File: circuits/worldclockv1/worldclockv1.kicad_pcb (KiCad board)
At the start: 2 copper layers, 152.4 x 76.2 mm, 98 parts, among them J1 Rotary Encoder Module, J2 UART, J3 Power, J4 Display 1 A, J5 Display 2 A, J6 Display 3 A, J7 Display 1 B, J8 Display 2 B, J9 Display 3 B, Q1 BSS138, Q2 BSS138, Q3 BSS138, Q4 BSS138, Q5 BSS138, Q6 BSS138, SW1 EN, SW2 BOOT, U1 ESP32-WROOM-32UE, U2 DS3232M, U3 LD1117S33TR_SOT223, U4 L7805, U5 L7805, U6 L7805, U7 LM386

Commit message: World Clock PCB completed
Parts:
- added C18: 100 nF, Capacitor_SMD:C_1206_3216Metric_Pad1.33x1.80mm_HandSolder, F.Cu at (201.7, 119.4)
- added F1: Polyfuse, Fuse:Fuseholder_Littelfuse_Nano2_157x, F.Cu at (195.6, 138.9)
- added Hole1: MountingHole_3.2mm_M3, MountingHole:MountingHole_3.2mm_M3, F.Cu at (46.2, 43.7)
- added Hole2: MountingHole_3.2mm_M3, MountingHole:MountingHole_3.2mm_M3, F.Cu at (229.9, 43.7)
- added Hole3: MountingHole_3.2mm_M3, MountingHole:MountingHole_3.2mm_M3, F.Cu at (46.2, 153.4)
- added Hole4: MountingHole_3.2mm_M3, MountingHole:MountingHole_3.2mm_M3, F.Cu at (229.9, 153.5)
- added J10: BOOT, Connector_PinHeader_2.54mm:PinHeader_1x02_P2.54mm_Vertical, F.Cu at (228.3, 95.8)
- added JP10: ID_WP, Jumper:SolderJumper-2_P1.3mm_Open_RoundedPad1.0x1.5mm, F.Cu at (189.1, 135.6)
- added JP7: ID_WP, Jumper:SolderJumper-2_P1.3mm_Open_RoundedPad1.0x1.5mm, F.Cu at (63.5, 73.2)
- added JP8: ID_WP, Jumper:SolderJumper-2_P1.3mm_Open_RoundedPad1.0x1.5mm, F.Cu at (63.5, 107.0)
- added JP9: ID_WP, Jumper:SolderJumper-2_P1.3mm_Open_RoundedPad1.0x1.5mm, F.Cu at (63.5, 141.2)
- added Q7: IRLML6402, Package_TO_SOT_SMD:SOT-23, F.Cu at (189.0, 141.8)
- added R23: 100k, Resistor_SMD:R_1206_3216Metric_Pad1.30x1.75mm_HandSolder, F.Cu at (189.0, 147.6)
- added R24: 10k, Resistor_SMD:R_1206_3216Metric_Pad1.30x1.75mm_HandSolder, F.Cu at (191.0, 112.8)
- added R25: 10k, Resistor_SMD:R_1206_3216Metric_Pad1.30x1.75mm_HandSolder, F.Cu at (191.0, 103.4)
- added R26: 10k, Resistor_SMD:R_1206_3216Metric_Pad1.30x1.75mm_HandSolder, F.Cu at (221.0, 116.1)
- added SW3: RotaryEncoder_Switch, Rotary_Encoder:RotaryEncoder_Alps_EC11E-Switch_Vertical_H20mm, F.Cu at (195.1, 105.7)
- added SW4: Alt, Button_Switch_THT:SW_PUSH_6mm, F.Cu at (214.5, 106.0)
- added TP25: GND, TestPoint:TestPoint_Loop_D2.50mm_Drill1.0mm, F.Cu at (87.4, 152.1)
- added TP26: GND, TestPoint:TestPoint_Loop_D2.50mm_Drill1.0mm, F.Cu at (95.8, 152.1)
- added TP27: GND, TestPoint:TestPoint_Loop_D2.50mm_Drill1.0mm, F.Cu at (104.3, 152.1)
- added TP28: GND, TestPoint:TestPoint_Loop_D2.50mm_Drill1.0mm, F.Cu at (112.8, 152.1)
- J3: footprint Connector_PinSocket_2.54mm:PinSocket_1x02_P2.54mm_Vertical -> Connector_BarrelJack:BarrelJack_Horizontal
- SW1, SW2: footprint Connector_PinSocket_2.54mm:PinSocket_1x02_P2.54mm_Vertical -> Button_Switch_THT:SW_PUSH_6mm
- moved TP15 524.4 mm to (185.2, 151.9)
- moved TP16 514.9 mm to (176.8, 151.9)
- moved TP17 508.1 mm to (171.8, 151.9)
- moved JP2 501.3 mm to (167.9, 151.9), turned to 180 degrees
- moved TP21 500.8 mm to (163.9, 151.9)
- moved J3 500.0 mm to (203.8, 144.1), turned to 90 degrees
- moved U3 498.1 mm to (149.4, 151.9), turned to 180 degrees
- moved JP1 497.5 mm to (181.0, 151.9), turned to 180 degrees
- moved C4 468.1 mm to (157.8, 151.8), turned to -90 degrees
- moved RV1 443.1 mm to (230.4, 85.8), turned to 180 degrees
- moved C8 441.9 mm to (140.2, 152.7), turned to -90 degrees
- moved RV2 437.4 mm to (217.2, 83.3), turned to 90 degrees
- moved TP20 429.6 mm to (66.0, 151.4)
- moved JP5 414.0 mm to (62.1, 151.4), turned to 180 degrees
- moved TP24 410.8 mm to (57.9, 151.4)
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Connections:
- net Net-(J1-Pin_1) renamed /Rotary Encoder Module/CLK
- net Net-(J1-Pin_2) renamed /Rotary Encoder Module/DT
- net Net-(J1-Pin_3) renamed /Rotary Encoder Module/SW
- JP1 pad 1: Net-(J3-Pin_1) -> Net-(JP1-A)
- R12 pad 1: +5V -> +5V #1
- R13 pad 1: +5V -> +5V #1
- R14 pad 1: +5V -> +5V #2
- R15 pad 1: +5V -> +5V #2
- R18 pad 1: +5V -> +5V #3
- R19 pad 1: +5V -> +5V #3
- TP15 pad 1: Net-(J3-Pin_1) -> Net-(JP1-A)
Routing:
- net +VDC: track 0.00 -> 452.5 mm
- net +3V3: track 0.00 -> 329.2 mm, vias 0 -> 10
- net +5V #1: track 0.00 -> 97.8 mm, vias 0 -> 3
- net +5V #2: track 0.00 -> 96.4 mm, vias 0 -> 3
- net +5V #3: track 0.00 -> 96.0 mm, vias 0 -> 3
- net /Rotary Encoder Module/DT: track 0.00 -> 86.9 mm, vias 0 -> 5
- net Net-(U1-IO26): track 0.00 -> 84.8 mm, vias 0 -> 4
- net /Rotary Encoder Module/SW: track 0.00 -> 84.2 mm, vias 0 -> 1
- net /Level Shifter/LV5: track 0.00 -> 78.8 mm
- net /Level Shifter/LV6: track 0.00 -> 78.6 mm
- net Net-(J10-Pin_1): track 0.00 -> 74.0 mm, vias 0 -> 3
- net Net-(U1-IO4): track 0.00 -> 73.0 mm, vias 0 -> 2
- net /Level Shifter/LV3: track 0.00 -> 72.9 mm, vias 0 -> 2
- net /Level Shifter/LV1: track 0.00 -> 72.9 mm
- net /Level Shifter/LV4: track 0.00 -> 70.7 mm, vias 0 -> 2
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- added copper zone on B.Cu, net GND
- added copper zone on F.Cu, net GND
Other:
- board size 152.4 x 76.2 mm -> 193.8 x 120 mm
- board text added: "3V3"
- board text added: "3V3 Current"
- board text added: "5V Current"
- board text added: "Audio"
- board text added: "Boot"
- board text added: "CLK"
- board text added: "DAC1"
- board text added: "DIO"
- board text added: "DT"
- board text added: "EN"
- board text added: "ESP32 World Clock v1.0"
- board text added: "GND"
- board text added: "GOS-WC-01 2026-04"
- board text added: "INT"
- board text added: "Mode"
- board text added: "Prog"
- board text added: "RST"
- board text added: "RX"
- board text added: "Reset"
- board text added: "Rot Enc"
- board text added: "SCL"
- board text added: "SDA"
- board text added: "SW"
- board text added: "TX"
- board text added: "Total Current"
- board text added: "© 2026 Geirmundur Orri Sigurdsson"

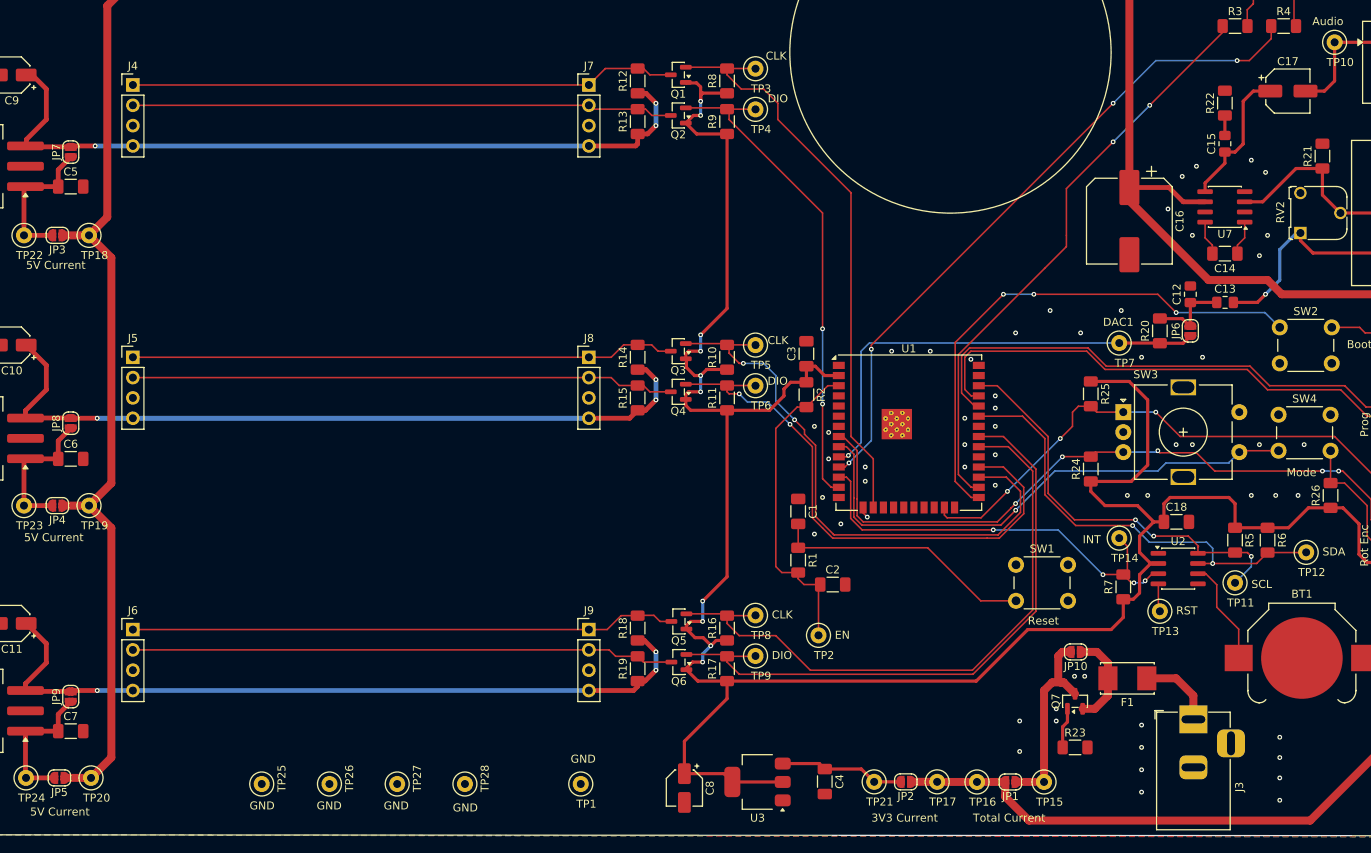
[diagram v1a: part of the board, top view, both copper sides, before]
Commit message: Update some caps footprint sizes for the World Clock
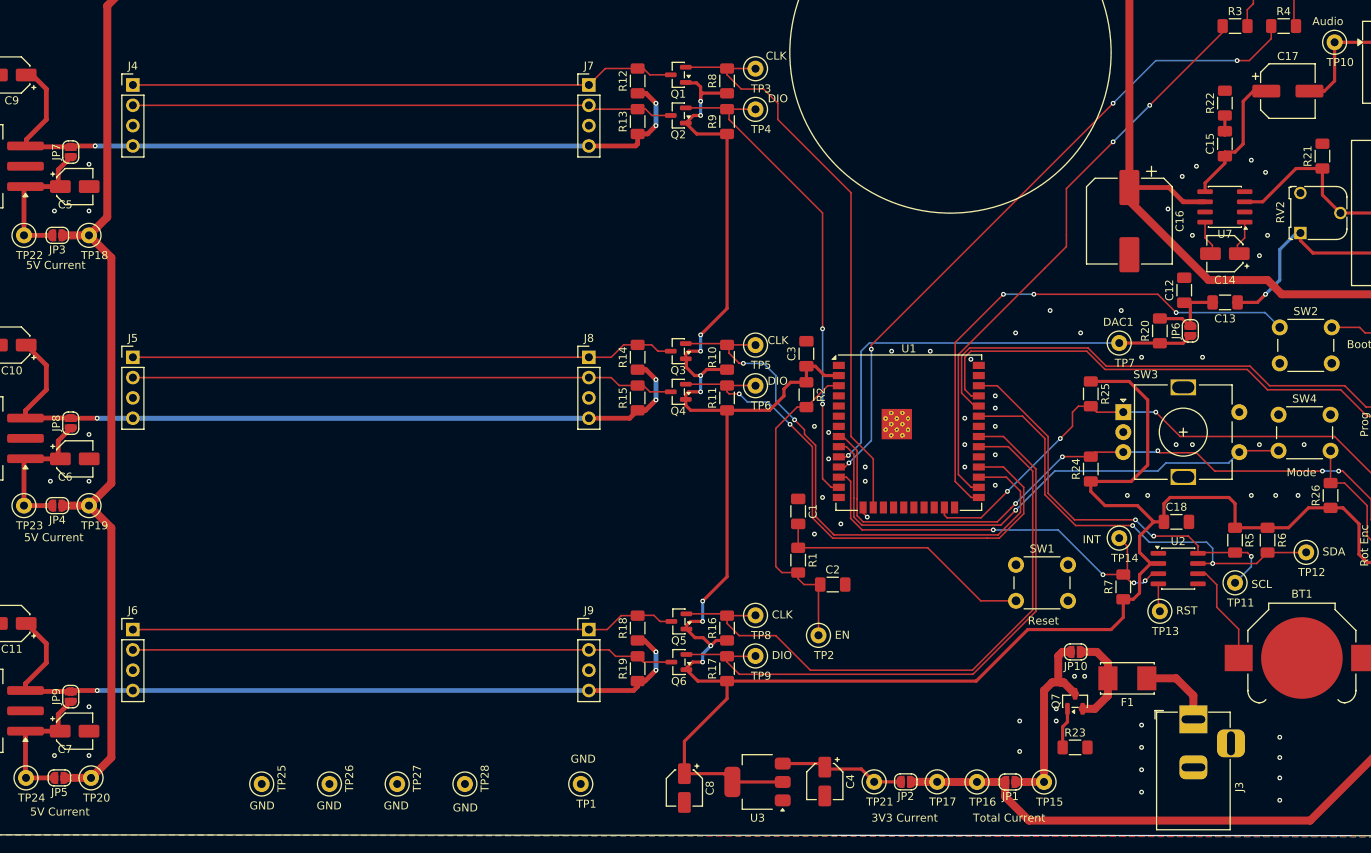
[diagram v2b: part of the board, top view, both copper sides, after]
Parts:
- C12, C13, C15: footprint Capacitor_SMD:C_0805_2012Metric_Pad1.18x1.45mm_HandSolder -> Capacitor_SMD:C_1206_3216Metric_Pad1.33x1.80mm_HandSolder
- C14, C4, C5, C6, C7: footprint Capacitor_SMD:C_1206_3216Metric_Pad1.33x1.80mm_HandSolder -> Capacitor_SMD:CP_Elec_4x5.4
- C17: footprint Capacitor_SMD:CP_Elec_5x5.4 -> Capacitor_SMD:CP_Elec_6.3x7.7
- moved C12 0.92 mm to (202.7, 90.4)
- moved C5 0.51 mm to (64.0, 77.5)
- moved C6 0.51 mm to (64.0, 111.5)
- moved C7 0.49 mm to (64.0, 145.5)
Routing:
- net GND: vias 63 -> 72

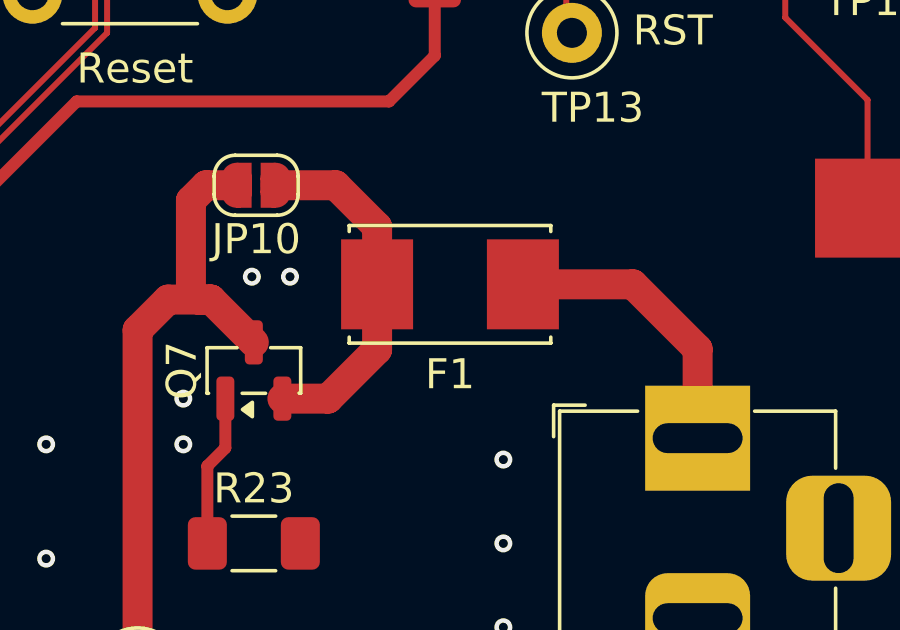
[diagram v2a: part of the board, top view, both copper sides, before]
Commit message: Update the footprint for the fuse and the layout on the PCB according for the World Clock
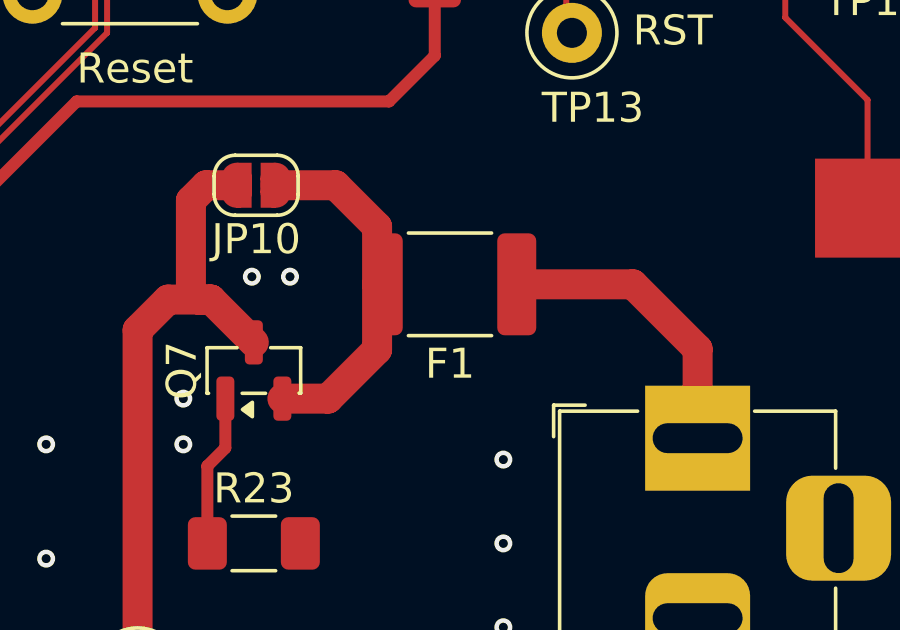
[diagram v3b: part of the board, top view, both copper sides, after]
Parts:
- F1: footprint Fuse:Fuseholder_Littelfuse_Nano2_157x -> Fuse:Fuse_1812_4532Metric_Pad1.30x3.40mm_HandSolder
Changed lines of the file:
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@@
 		)
 	)
-	(footprint "Fuse:Fuseholder_Littelfuse_Nano2_157x"
+	(footprint "Fuse:Fuse_1812_4532Metric_Pad1.30x3.40mm_HandSolder"
 		(layer "F.Cu")
 		(at 195.58 138.938 180)
-		(descr "Littelfuse NANO2 holder, https://www.littelfuse.com/~/media/electronics/datasheets/fuses/littelfuse_fuse_157_datasheet.pdf.pdf")
-		(tags "SMD Nano2 holder")
+		(descr "Fuse SMD 1812 (4532 Metric), square (rectangular) end terminal, IPC-7351 nominal with elongated pad for handsoldering. (Body size source: https://www.nikhef.nl/pub/departments/mt/projects/detectorR_D/dtddice/ERJ2G.pdf), generated with kicad-footprint-generator")
+		(tags "fuse handsolder")
 		(property "Reference" "F1"
-			(at 0 -3 0)
+			(at 0 -2.65 180)
 			(layer "F.SilkS")
 			(effects
@@
 		)
 		(property "Value" "Polyfuse"
-			(at 0 3 0)
+			(at 0 2.65 180)
 			(layer "F.Fab")
 			(effects
@@
 		(property "Datasheet" "~"
 			(at 0 0 180)
-			(unlocked yes)
 			(layer "F.Fab")
 			(hide yes)
@@
 		(property "Description" "Resettable fuse, polymeric positive temperature coefficient"
 			(at 0 0 180)
-			(unlocked yes)
 			(layer "F.Fab")
 			(hide yes)
@@
 		(attr smd)
 		(fp_line
-			(start 3.36 1.76)
-			(end 3.36 1.96)
+			(start -1.386252 1.71)
+			(end 1.386252 1.71)
 			(stroke
 				(width 0.12)
@@
 		)
 		(fp_line
-			(start 3.36 -1.96)
-			(end 3.36 -1.76)
+			(start -1.386252 -1.71)
+			(end 1.386252 -1.71)
 			(stroke
 				(width 0.12)
@@
 		)
 		(fp_line
-			(start -3.36 1.96)
-			(end 3.36 1.96)
-			(stroke
-				(width 0.12)
-				(type solid)
-			)
-			(layer "F.SilkS")
-		)
-		(fp_line
-			(start -3.36 1.76)
-			(end -3.36 1.96)
-			(stroke
-				(width 0.12)
-				(type solid)
-			)
-			(layer "F.SilkS")
-		)
-		(fp_line
-			(start -3.36 -1.96)
-			(end 3.36 -1.96)
-			(stroke
-				(width 0.12)
-				(type solid)
-			)
-			(layer "F.SilkS")
-		)
-		(fp_line
-			(start -3.36 -1.96)
-			(end -3.36 -1.76)
-			(stroke
-				(width 0.12)
-				(type solid)
-			)
-			(layer "F.SilkS")
-		)
-		(fp_line
-			(start 3.88 -2.1)
-			(end 3.88 2.1)
+			(start 3.13 1.95)
+			(end -3.13 1.95)
 			(stroke
 				(width 0.05)
@@
 		)
 		(fp_line
-			(start -3.88 2.1)
-			(end 3.88 2.1)
+			(start 3.13 -1.95)
+			(end 3.13 1.95)
 			(stroke
 				(width 0.05)
@@
 		)
 		(fp_line
-			(start -3.88 -2.1)
-			(end 3.88 -2.1)
+			(start -3.13 1.95)
+			(end -3.13 -1.95)
 			(stroke
 				(width 0.05)
@@
 		)
 		(fp_line
-			(start -3.88 -2.1)
-			(end -3.88 2.1)
+			(start -3.13 -1.95)
+			(end 3.13 -1.95)
 			(stroke
 				(width 0.05)
@@
 		)
 		(fp_line
-			(start 3.25 -1.85)
-			(end 3.25 1.85)
+			(start 2.25 1.6)
+			(end -2.25 1.6)
 			(stroke
 				(width 0.1)
@@
 		)
 		(fp_line
-			(start -3.25 1.85)
-			(end 3.25 1.85)
+			(start 2.25 -1.6)
+			(end 2.25 1.6)
 			(stroke
 				(width 0.1)
@@
 		)
 		(fp_line
-			(start -3.25 -1.85)
-			(end 3.25 -1.85)
+			(start -2.25 1.6)
+			(end -2.25 -1.6)
 			(stroke
 				(width 0.1)
@@
 		)
 		(fp_line
-			(start -3.25 -1.85)
-			(end -3.25 1.85)
+			(start -2.25 -1.6)
+			(end 2.25 -1.6)
 			(stroke
 				(width 0.1)
@@
 		)
 		(fp_text user "${REFERENCE}"
-			(at 0 0 0)
+			(at 0 0 180)
 			(layer "F.Fab")
 			(effects
@@
 			)
 		)
-		(pad "1" smd rect
-			(at -2.43 0 180)
-			(size 2.4 3)
+		(pad "1" smd roundrect
+			(at -2.225 0 180)
+			(size 1.3 3.4)
 			(layers "F.Cu" "F.Mask" "F.Paste")
+			(roundrect_rratio 0.192308)
 			(net 25 "Net-(J3-Pin_1)")
 			(pintype "passive")
 		)
-		(pad "2" smd rect
-			(at 2.43 0 180)
-			(size 2.4 3)
+		(pad "2" smd roundrect
+			(at 2.225 0 180)
+			(size 1.3 3.4)
 			(layers "F.Cu" "F.Mask" "F.Paste")
+			(roundrect_rratio 0.192308)
 			(net 44 "Net-(JP10-A)")
 			(pintype "passive")
 		)
 		(embedded_fonts no)
-		(model "${KICAD9_3DMODEL_DIR}/Fuse.3dshapes/Fuseholder_Littelfuse_Nano2_157x.step"
+		(model "${KICAD9_3DMODEL_DIR}/Fuse.3dshapes/Fuse_1812_4532Metric.step"
 			(offset
 				(xyz 0 0 0)
